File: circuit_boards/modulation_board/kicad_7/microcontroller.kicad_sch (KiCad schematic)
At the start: 21 parts

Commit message: Progress on circuit boards
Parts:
- added C306, C309: 100n, Capacitor_SMD:C_0603_1608Metric, symbol Device:C
- added C307: 1u, Capacitor_SMD:C_0805_2012Metric, symbol Device:C
- added C308, C310: 10u, Capacitor_SMD:C_0805_2012Metric, symbol Device:C
- FB301, FB302, FB303, FB304: renamed from FB?; footprint (none) -> Inductor_SMD:L_0805_2012Metric
- R301, R302, R303, R305, R306: renamed from R?; footprint Resistor_SMD:R_0805_2012Metric -> Resistor_SMD:R_0603_1608Metric
- R304: renamed from R?; value 1k -> 220; footprint Resistor_SMD:R_0805_2012Metric -> Resistor_SMD:R_0603_1608Metric
- gave numbers to parts that had none: 11
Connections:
- net GATE is gone; now on net ~{CS_0}: U1.25 (PA15)
- net +3.3V: now also C306.1, C307.1, C308.1
- net +3.3VA: now also C309.1, C310.1
- net GND: now also C306.2, C307.2, C308.2, C309.2, C310.2
- net MIDI_IN_P4: now also FB301.1; no longer R301.1
- net MODOSC_SQR: now also U1.21 (PA11)
- net PWM_LFO_SQR: now also U1.22 (PA12)
- net ~{CS_0}: no longer U1.27 (PB4)
- net ~{EXT_GATE}: now also U1.18 (PA8)
- net at D301.1 (K), U2.2 (A): now also R301.2; no longer FB301.2
- net MIDI_TX: no longer names the net of U1.19 (PA9)
- new net: FB301.2, R301.1
- no-connect marks 1 -> 6
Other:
- moved on the sheet: C301, C302, C303, FB301, FB302, R301, R302, U1, Y301

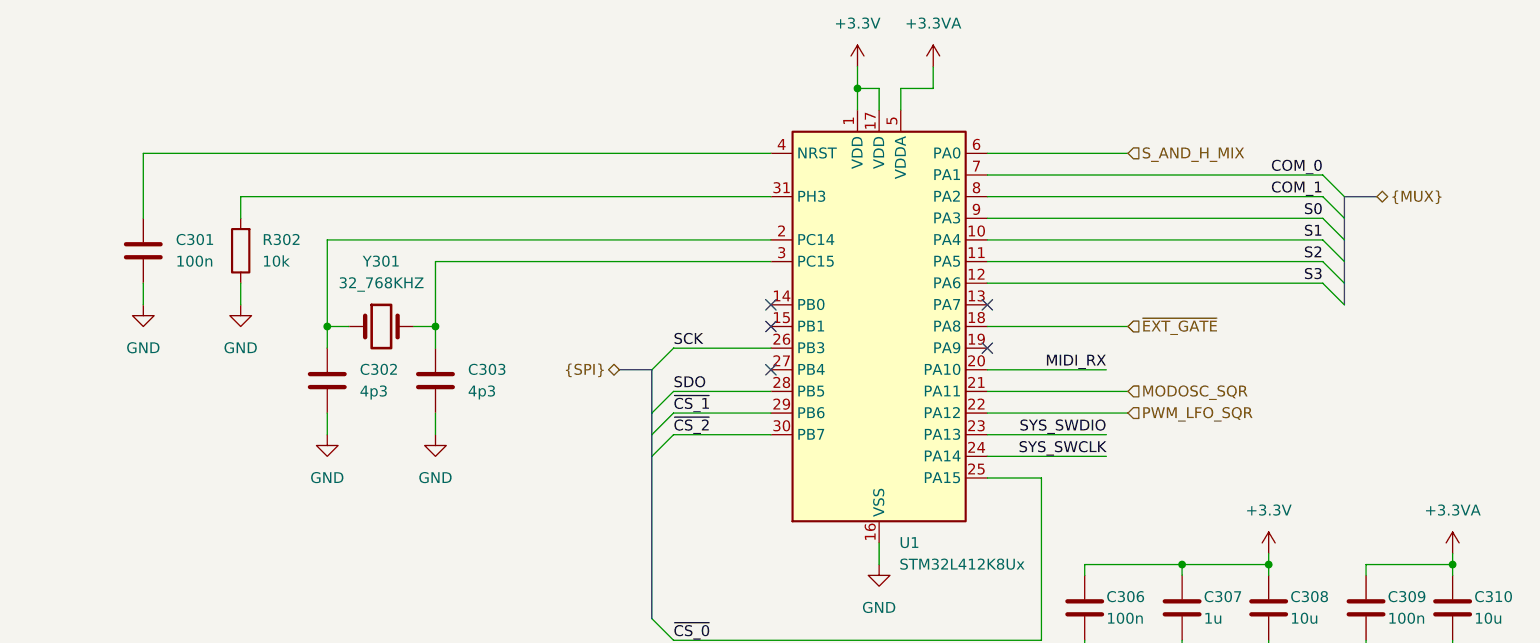
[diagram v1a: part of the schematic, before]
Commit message: Tweaks to mod board, add debug pin
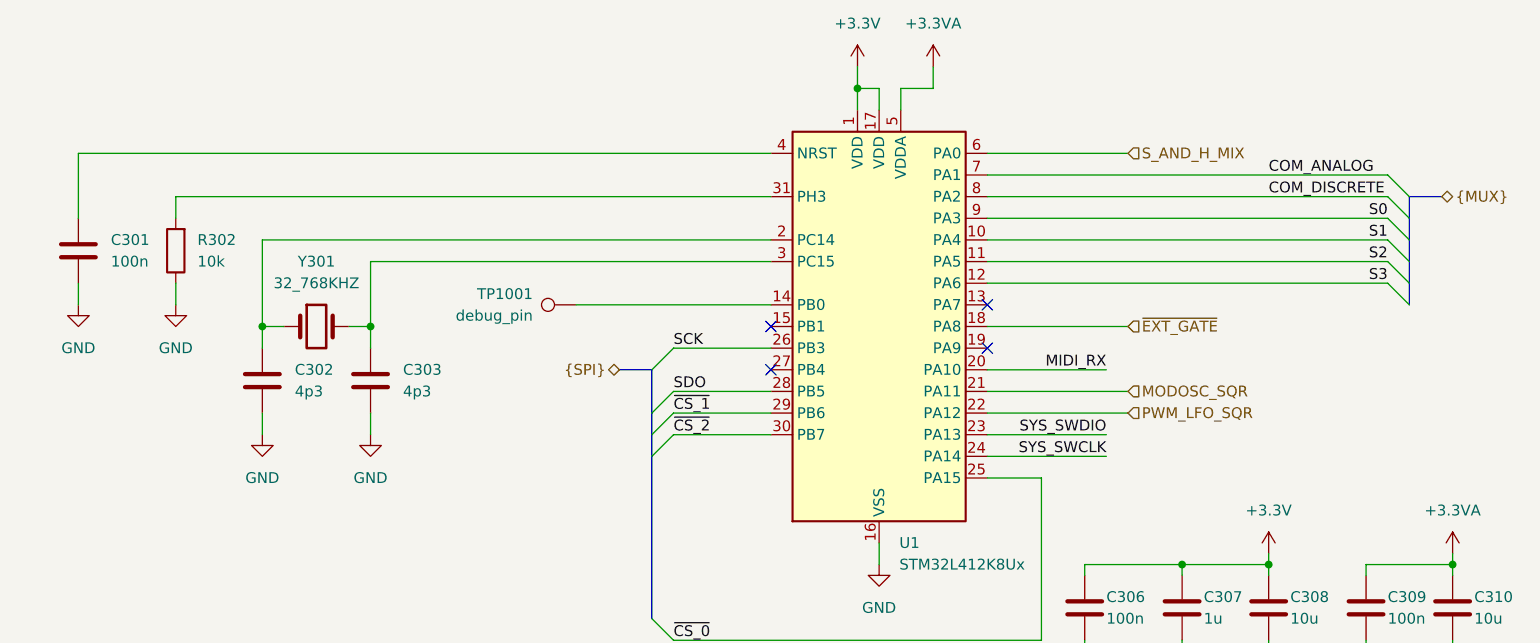
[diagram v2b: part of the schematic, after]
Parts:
- added TP1001: debug_pin, TestPoint:TestPoint_Keystone_5000-5004_Miniature, symbol Connector:TestPoint
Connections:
- net at U1.14 (PB0): now also TP1001.1
- net COM_0 renamed COM_ANALOG
- net COM_1 renamed COM_DISCRETE
- no-connect marks 6 -> 5
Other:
- moved on the sheet: C301, C302, C303, R302, Y301
